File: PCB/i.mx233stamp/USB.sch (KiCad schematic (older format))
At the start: 38 parts, among them J3 USB_2A, J4 USB_2A, U4 GL850G, U5 RCLAMP0502B, U6 RCLAMP0502B, U7 RCLAMP0502B, U8 RCLAMP0502B, U9 MCP130, X2 12MHz

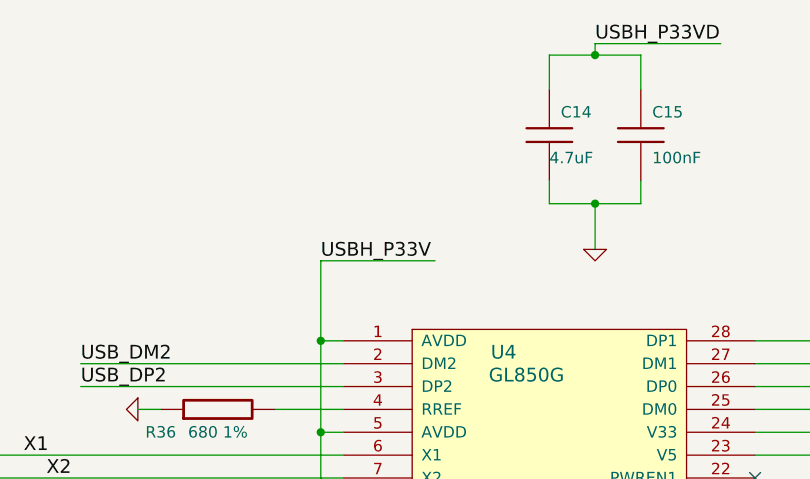
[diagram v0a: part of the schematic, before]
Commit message: Arreglando la falta de conexión del HUB usb
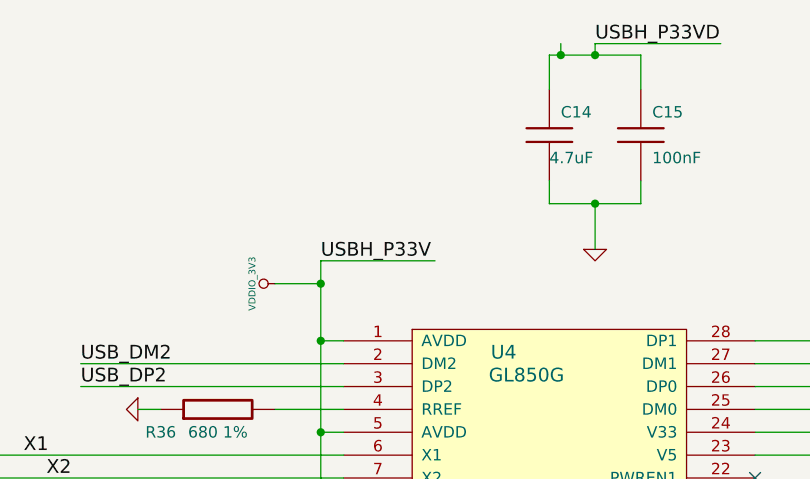
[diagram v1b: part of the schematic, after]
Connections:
- net labels added: VDDIO_3V3
- wire segments 145 -> 147
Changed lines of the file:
@@
-EESchema Schematic File Version 2  date Fri 26 Aug 2011 09:24:05 AM COT
+EESchema Schematic File Version 2  date Mon 29 Aug 2011 10:09:29 AM COT
 LIBS:con-jack
 LIBS:adm3101e
@@
 Sheet 2 4
 Title ""
-Date "26 aug 2011"
+Date "29 aug 2011"
 Rev ""
 Comp ""
@@
 Comment4 ""
 $EndDescr
+Connection ~ 7300 1800
+Wire Wire Line
+	7100 1800 7300 1800
 Wire Wire Line
 	1900 1600 1900 2000
@@
 	5800 3550 5850 3550
 Connection ~ 5850 3550
+Wire Wire Line
+	8350 750  8350 800
+Connection ~ 8350 800
+$Comp
+L VDDIO_3V3 #PWR01
+U 1 1 4E5BAA82
+P 7100 1800
+F 0 "#PWR01" H 7100 1900 30  0001 C CNN
+F 1 "VDDIO_3V3" H 7100 1900 30  0000 C CNN
+	1    7100 1800
+	0    -1   -1   0
+$EndComp
 Text GLabel 1900 2000 3    60   BiDi ~ 0
 GND_CASE
@@
 $EndComp
 $Comp
-L GND #PWR12
+L GND #PWR02
 U 1 1 4E43139E
 P 5550 3250
-F 0 "#PWR12" H 5550 3250 30  0001 C CNN
+F 0 "#PWR02" H 5550 3250 30  0001 C CNN
 F 1 "GND" H 5550 3180 30  0001 C CNN
 	1    5550 3250
@@
 USBH_P33VD
 $Comp
-L GND #PWR16
+L GND #PWR03
 U 1 1 4E41C8A5
 P 7300 3400
-F 0 "#PWR16" H 7300 3400 30  0001 C CNN
+F 0 "#PWR03" H 7300 3400 30  0001 C CNN
 F 1 "GND" H 7300 3330 30  0001 C CNN
 	1    7300 3400
@@
 $EndComp
 $Comp
-L GND #PWR14
+L GND #PWR04
 U 1 1 4E41C7BC
 P 6100 3800
-F 0 "#PWR14" H 6100 3800 30  0001 C CNN
+F 0 "#PWR04" H 6100 3800 30  0001 C CNN
 F 1 "GND" H 6100 3730 30  0001 C CNN
 	1    6100 3800
@@
 $EndComp
 $Comp
-L GND #PWR8
+L GND #PWR05
 U 1 1 4E4157F8
 P 4250 4850
-F 0 "#PWR8" H 4250 4850 30  0001 C CNN
+F 0 "#PWR05" H 4250 4850 30  0001 C CNN
 F 1 "GND" H 4250 4780 30  0001 C CNN
 	1    4250 4850
@@
 $EndComp
 $Comp
-L GND #PWR7
+L GND #PWR06
 U 1 1 4E4157E9
 P 4250 3800
-F 0 "#PWR7" H 4250 3800 30  0001 C CNN
+F 0 "#PWR06" H 4250 3800 30  0001 C CNN
 F 1 "GND" H 4250 3730 30  0001 C CNN
 	1    4250 3800
@@
 $EndComp
 $Comp
-L GND #PWR10
+L GND #PWR07
 U 1 1 4E4157C0
 P 4300 2650
-F 0 "#PWR10" H 4300 2650 30  0001 C CNN
+F 0 "#PWR07" H 4300 2650 30  0001 C CNN
 F 1 "GND" H 4300 2580 30  0001 C CNN
 	1    4300 2650
@@
 $EndComp
 $Comp
-L GND #PWR9
+L GND #PWR08
 U 1 1 4E4157B3
 P 4300 1350
-F 0 "#PWR9" H 4300 1350 30  0001 C CNN
+F 0 "#PWR08" H 4300 1350 30  0001 C CNN
 F 1 "GND" H 4300 1280 30  0001 C CNN
 	1    4300 1350
@@
 $EndComp
 $Comp
-L GND #PWR4
+L GND #PWR09
 U 1 1 4E41559E
 P 1400 3350
-F 0 "#PWR4" H 1400 3350 30  0001 C CNN
+F 0 "#PWR09" H 1400 3350 30  0001 C CNN
 F 1 "GND" H 1400 3280 30  0001 C CNN
 	1    1400 3350
@@
 $EndComp
 $Comp
-L GND #PWR3
+L GND #PWR010
 U 1 1 4E415157
 P 1400 2050
-F 0 "#PWR3" H 1400 2050 30  0001 C CNN
+F 0 "#PWR010" H 1400 2050 30  0001 C CNN
 F 1 "GND" H 1400 1980 30  0001 C CNN
 	1    1400 2050
@@
 $EndComp
 $Comp
-L VDD5V #PWR2
+L VDD5V #PWR011
 U 1 1 4E414F5E
 P 950 2450
-F 0 "#PWR2" H 950 2550 30  0001 C CNN
+F 0 "#PWR011" H 950 2550 30  0001 C CNN
 F 1 "VDD5V" H 950 2550 30  0000 C CNN
 	1    950  2450
@@
 $EndComp
 $Comp
-L GND #PWR6
+L GND #PWR012
 U 1 1 4E414F5D
 P 2750 3350
-F 0 "#PWR6" H 2750 3350 30  0001 C CNN
+F 0 "#PWR012" H 2750 3350 30  0001 C CNN
 F 1 "GND" H 2750 3280 30  0001 C CNN
 	1    2750 3350
@@
 $EndComp
 $Comp
-L GND #PWR5
+L GND #PWR013
 U 1 1 4E414F30
 P 2700 2100
-F 0 "#PWR5" H 2700 2100 30  0001 C CNN
+F 0 "#PWR013" H 2700 2100 30  0001 C CNN
 F 1 "GND" H 2700 2030 30  0001 C CNN
 	1    2700 2100
@@
 $EndComp
 $Comp
-L VDD5V #PWR1
+L VDD5V #PWR014
 U 1 1 4E414E3D
 P 950 1150
-F 0 "#PWR1" H 950 1250 30  0001 C CNN
+F 0 "#PWR014" H 950 1250 30  0001 C CNN
 F 1 "VDD5V" H 950 1250 30  0000 C CNN
 	1    950  1150
@@
 $EndComp
 $Comp
-L GND #PWR25
+L GND #PWR015
 U 1 1 4E3C4430
 P 10750 3150
-F 0 "#PWR25" H 10750 3150 30  0001 C CNN
+F 0 "#PWR015" H 10750 3150 30  0001 C CNN
 F 1 "GND" H 10750 3080 30  0001 C CNN
 	1    10750 3150
@@
 $EndComp
 $Comp
-L VDD5V #PWR24
+L VDD5V #PWR016
 U 1 1 4E3C4429
 P 10750 2550
-F 0 "#PWR24" H 10750 2650 30  0001 C CNN
+F 0 "#PWR016" H 10750 2650 30  0001 C CNN
 F 1 "VDD5V" H 10750 2650 30  0000 C CNN
 	1    10750 2550
@@
 $EndComp
 $Comp
-L VDD5V #PWR20
+L VDD5V #PWR017
 U 1 1 4E3C4418
 P 9600 2550
-F 0 "#PWR20" H 9600 2650 30  0001 C CNN
+F 0 "#PWR017" H 9600 2650 30  0001 C CNN
 F 1 "VDD5V" H 9600 2650 30  0000 C CNN
 	1    9600 2550
@@
 $EndComp
 $Comp
-L GND #PWR18
+L GND #PWR018
 U 1 1 4E3C436B
 P 8500 1650
-F 0 "#PWR18" H 8500 1650 30  0001 C CNN
+F 0 "#PWR018" H 8500 1650 30  0001 C CNN
 F 1 "GND" H 8500 1580 30  0001 C CNN
 	1    8500 1650
@@
 USBH_P33V
 $Comp
-L VDD5V #PWR21
+L VDD5V #PWR019
 U 1 1 4E3C4207
 P 9600 2950
-F 0 "#PWR21" H 9600 3050 30  0001 C CNN
+F 0 "#PWR019" H 9600 3050 30  0001 C CNN
 F 1 "VDD5V" H 9600 3050 30  0000 C CNN
 	1    9600 2950
@@
 USBH_P33V
 $Comp
-L GND #PWR22
+L GND #PWR020
 U 1 1 4E3C3A60
 P 9900 5600
-F 0 "#PWR22" H 9900 5600 30  0001 C CNN
+F 0 "#PWR020" H 9900 5600 30  0001 C CNN
 F 1 "GND" H 9900 5530 30  0001 C CNN
 	1    9900 5600
@@
 $EndComp
 $Comp
-L GND #PWR17
+L GND #PWR021
 U 1 1 4E3C3A56
 P 8000 5600
-F 0 "#PWR17" H 8000 5600 30  0001 C CNN
+F 0 "#PWR021" H 8000 5600 30  0001 C CNN
 F 1 "GND" H 8000 5530 30  0001 C CNN
 	1    8000 5600
@@
 andres.calderon@emqbit.com\n
 $Comp
-L GND #PWR15
+L GND #PWR022
 U 1 1 4E3C3807
 P 6500 2350
-F 0 "#PWR15" H 6500 2350 30  0001 C CNN
+F 0 "#PWR022" H 6500 2350 30  0001 C CNN
 F 1 "GND" H 6500 2280 30  0001 C CNN
 	1    6500 2350
@@
 $EndComp
 $Comp
-L GND #PWR23
+L GND #PWR023
 U 1 1 4E3C36BE
 P 10400 3600
-F 0 "#PWR23" H 10400 3600 30  0001 C CNN
+F 0 "#PWR023" H 10400 3600 30  0001 C CNN
 F 1 "GND" H 10400 3530 30  0001 C CNN
 	1    10400 3600
@@
 X1
 $Comp
-L GND #PWR19
+L GND #PWR024
 U 1 1 4E3C222B
 P 9500 3750
-F 0 "#PWR19" H 9500 3750 30  0001 C CNN
+F 0 "#PWR024" H 9500 3750 30  0001 C CNN
 F 1 "GND" H 9500 3680 30  0001 C CNN
 	1    9500 3750
@@
 USB_DM2
 $Comp
-L GND #PWR11
+L GND #PWR025
 U 1 1 4E3C212B
 P 5250 4300
-F 0 "#PWR11" H 5250 4300 30  0001 C CNN
+F 0 "#PWR025" H 5250 4300 30  0001 C CNN
 F 1 "GND" H 5250 4230 30  0001 C CNN
 	1    5250 4300
@@
 $EndComp
 $Comp
-L GND #PWR13
+L GND #PWR026
 U 1 1 4E3C206C
 P 5850 4300
-F 0 "#PWR13" H 5850 4300 30  0001 C CNN
+F 0 "#PWR026" H 5850 4300 30  0001 C CNN
 F 1 "GND" H 5850 4230 30  0001 C CNN
 	1    5850 4300

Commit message: error de mascara
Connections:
- wire segments 147 -> 146

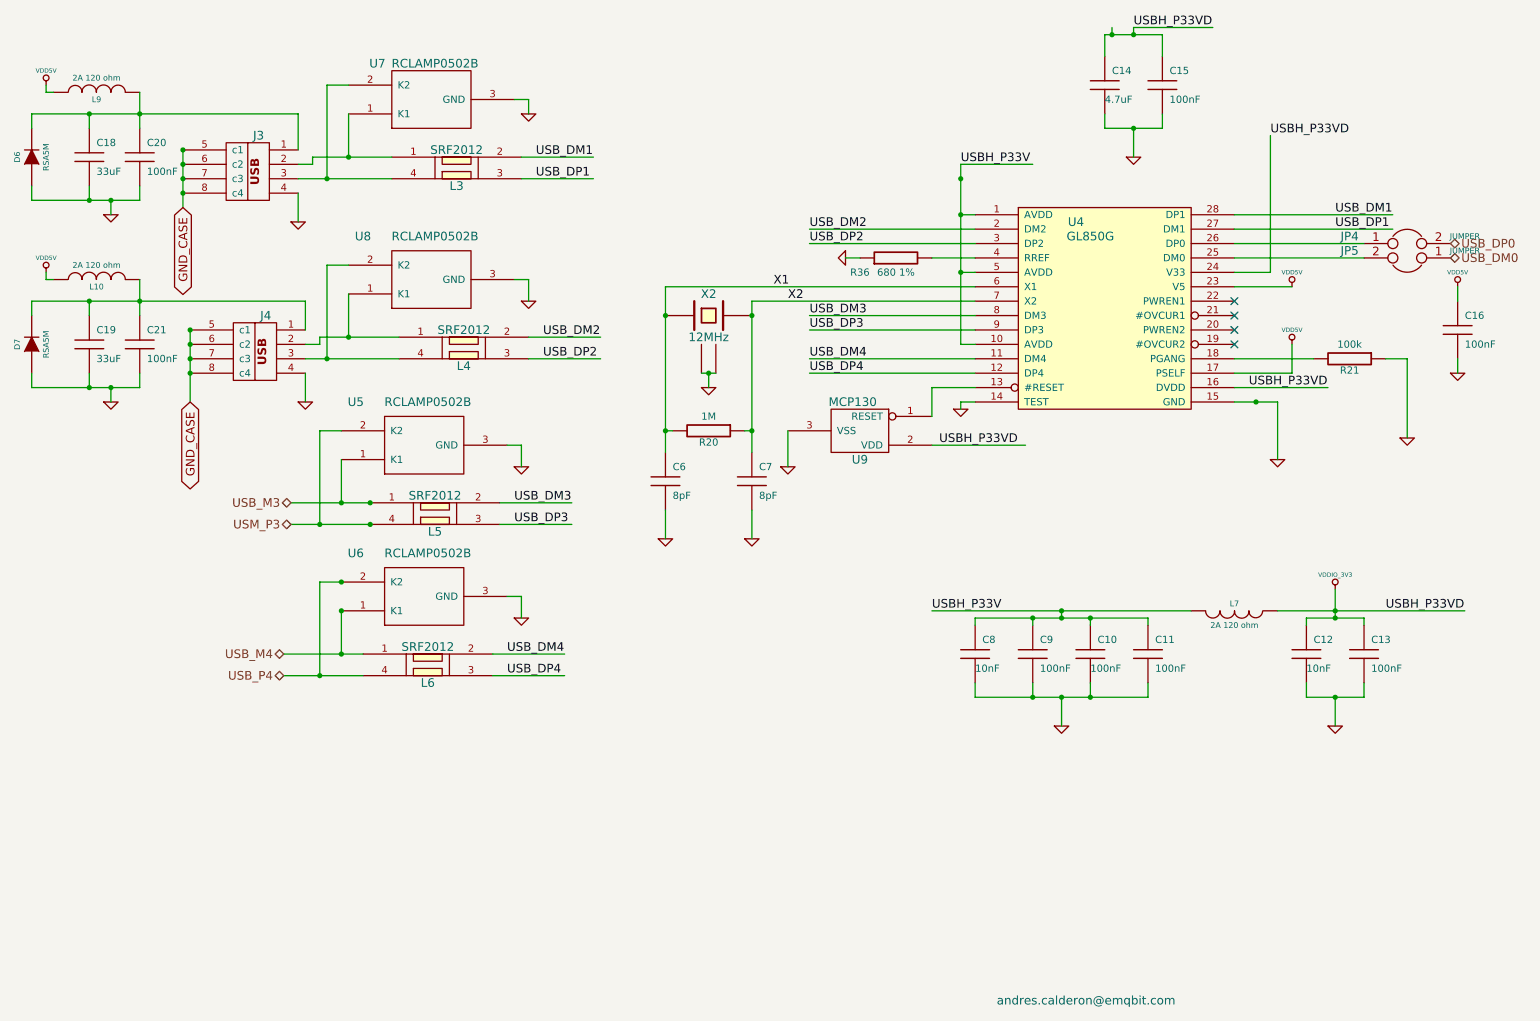
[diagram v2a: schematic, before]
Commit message: Cambio del footprint de la M25P32, inversion de las señales del USB D+ D- asociadas a J3 TODO: remplazo del POR del hub USB por una resistencia de pull-up o cambio de footprint del POR
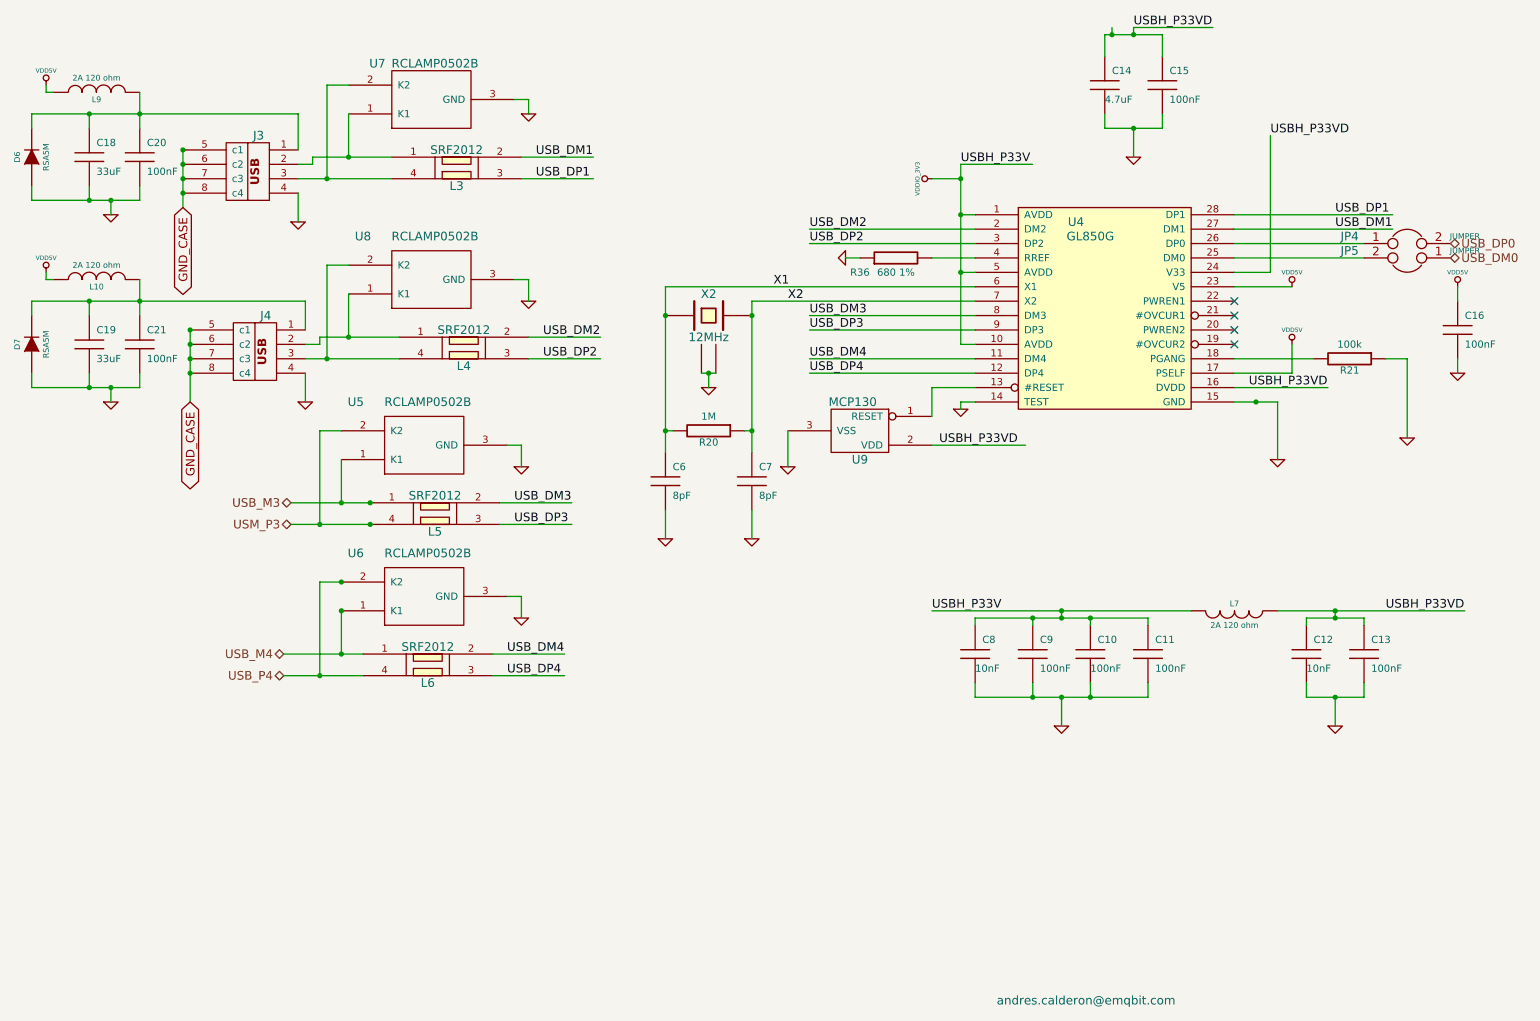
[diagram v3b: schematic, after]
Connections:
- wire segments 146 -> 147
